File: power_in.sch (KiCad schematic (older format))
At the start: 1 part

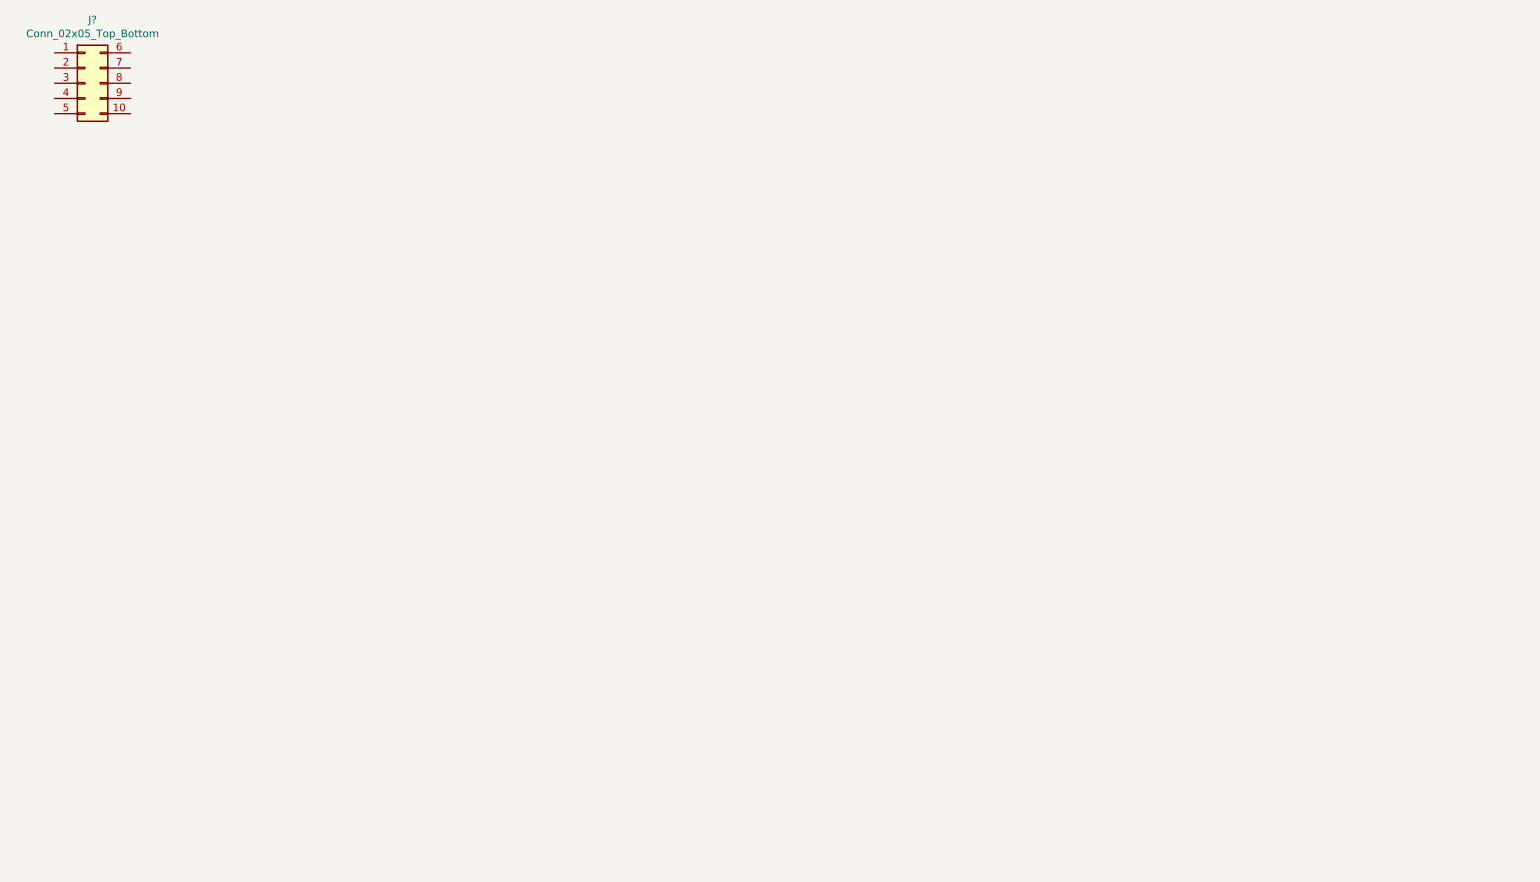
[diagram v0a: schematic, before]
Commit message: 3.3v LDO power
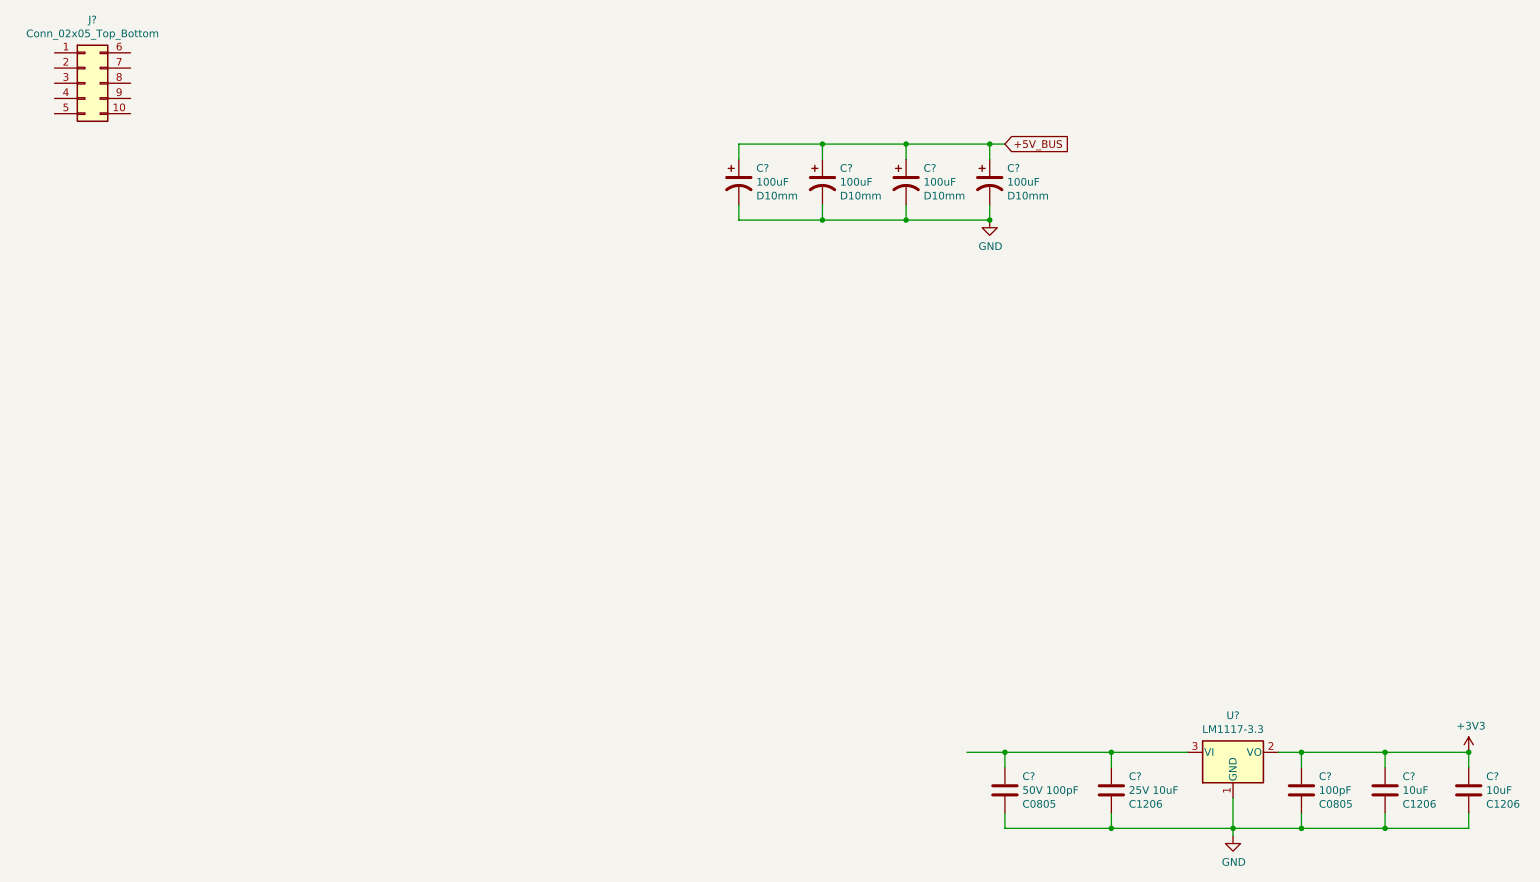
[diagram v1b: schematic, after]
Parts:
- added C? (x4): 100uF, Capacitor_THT:CP_Radial_D10.0mm_P2.50mm_P5.00mm, symbol Device:CP1
- added C?: 100pF, Capacitor_SMD:C_0805_2012Metric, symbol Device:C
- added C? (x2): 10uF, Capacitor_SMD:C_1206_3216Metric, symbol Device:C
- added C?: 25V 10uF, Capacitor_SMD:C_1206_3216Metric, symbol Device:C
- added C?: 50V 100pF, Capacitor_SMD:C_0805_2012Metric, symbol Device:C
- added U?: LM1117-3.3, Package_TO_SOT_SMD:SOT-223-3_TabPin2, symbol Regulator_Linear:LM1117-3.3
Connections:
- net labels added: +3V3, +5V_BUS, GND
- wire segments 0 -> 38
